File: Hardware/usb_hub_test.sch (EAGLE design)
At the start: 99 parts, among them CN1 54819-0519, CN2 TSW-120-08-L-S-RA, CN4 1-1734530-1, IC1 FT230XQ, IC2 TUSB2046BIRHBT, IC3 MAX3375, IC4 PIC24FJ128GA202-I/MM, IC5 FT230XQ, IC7 MAX3375

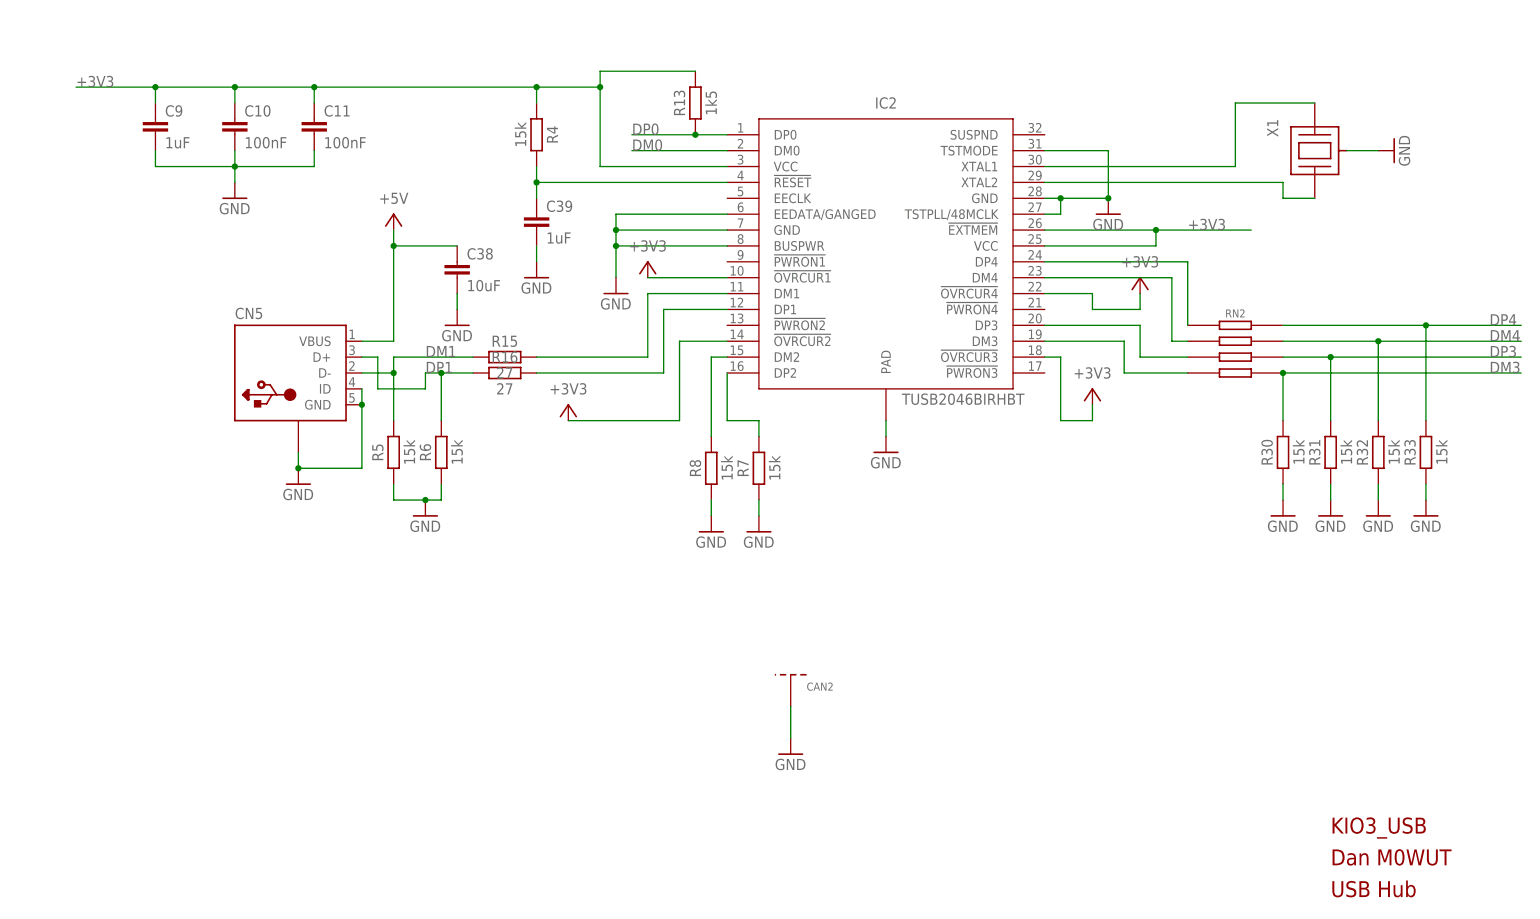
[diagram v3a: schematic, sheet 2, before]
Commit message: Implementing Board changes from v1
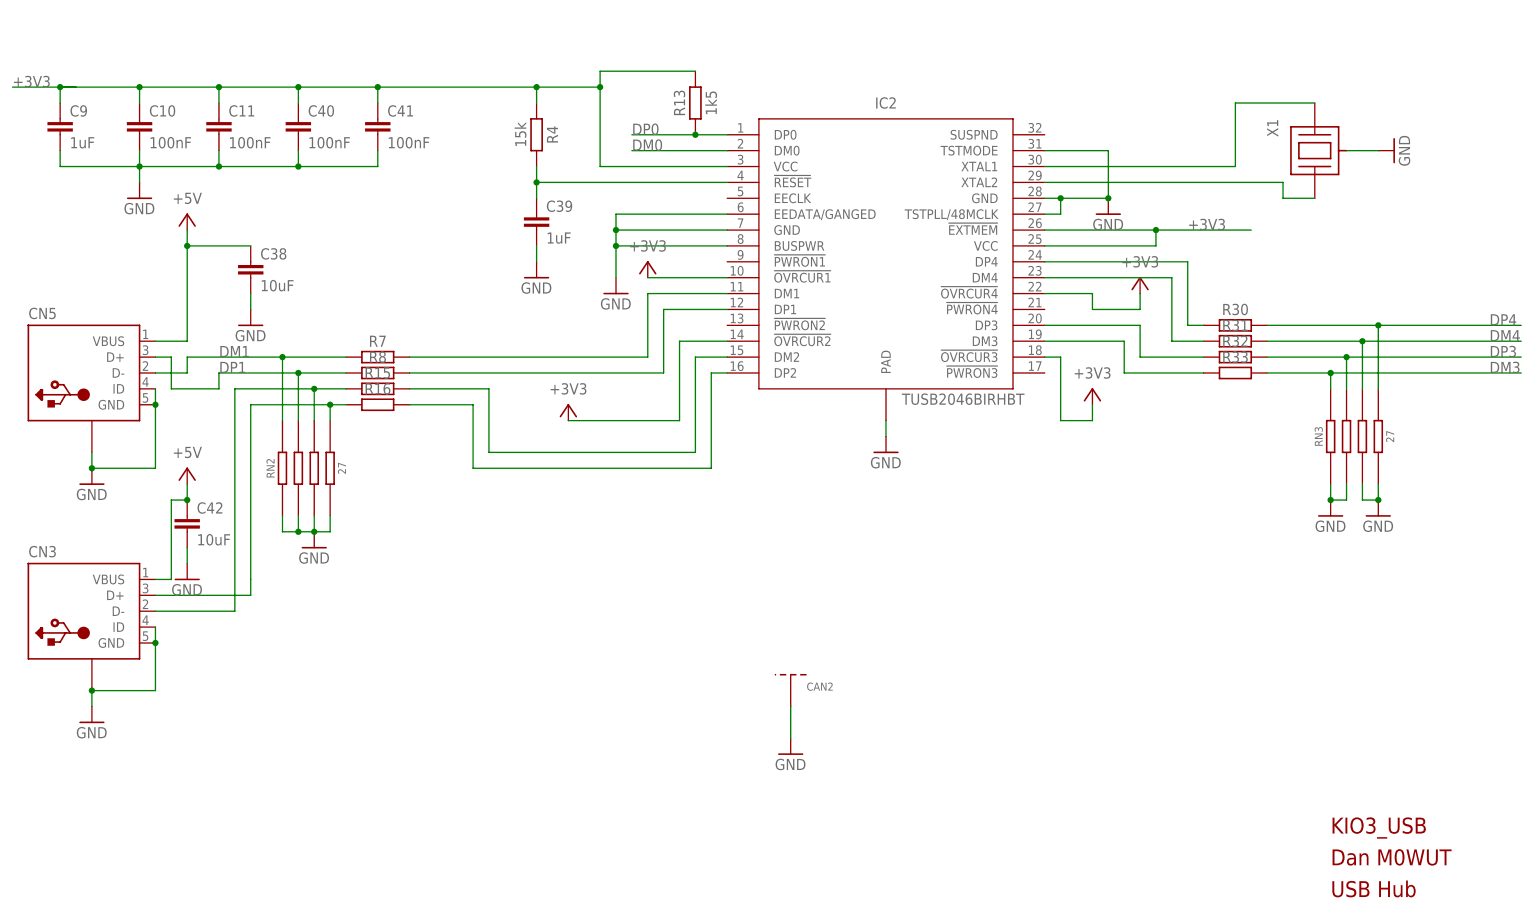
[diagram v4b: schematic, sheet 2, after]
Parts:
- removed C1, C35, C37: 100nF, rcl:C-EUC0402
- removed C27, C28, C33, C34: 1nF, rcl:C-EUC0402
- removed D2, D3: BZT52C4V7-7-F, adafruit:DIODESOD-123
- removed IC3, IC7: MAX3375, m0wut:IC_MAX3375
- removed L2, L3, L5, L6: 100uH, m0wut:INDUCTOR
- removed R12, R3: 220, rcl:R-EU_R0402
- removed R5, R6: 15k, rcl:R-EU_R0402
- added C40, C41: 100nF, rcl:C-EUC0402
- added C42: 10uF, rcl:C-EUC0805
- added CN3: (no value), m0wut:USBOTG_VERTICAL
- added Q1, Q2: (no value), adafruit:MOSFET-NREFLOW
- added RN3: 27, m0wut:R_BOURNS_CAY16-J4
- added RN4: (no value), m0wut:R_BOURNS_CAY16-J4
- R15, R16: value 27 -> (none)
- R30, R31, R32, R33, R7, R8: value 15k -> (none)
- RN2: value (none) -> 27
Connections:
- removed net N$188: IC3.OH, L2.1
- removed net N$189: D2.C, IC3.IH, R12.1
- removed net N$4: D3.C, IC7.IH, R3.1
- removed net N$5: IC7.OH, L5.1
- removed net N$6: L3.1, R12.2
- removed net N$7: L6.1, R3.2
- removed net P3_RXD: C27.1, L5.2, U$1.1
- removed net P3_TXD: C28.1, L6.2, U$1.3
- new net N$18: CN3.D-, R15.1, RN2.3A
- new net N$19: CN3.D+, R16.1, RN2.4A
- net +3V3: now also C40.1, C41.1, RN4.2A; no longer C1.1, C35.1, IC3.EN, IC3.VL, IC7.EN, IC7.VL
- net +5V: now also C42.1, CN3.VBUS, RN4.3A; no longer C37.1, IC3.VH, IC7.VH
- net 232_RXD: now also Q2.G, RN4.1; no longer C33.1, L2.2
- net 232_TXD: now also Q1.D, RN4.3; no longer C34.1, L3.2
- net DM1: now also R7.1, RN2.1A; no longer R15.1, R5.2
- net DM3: now also R33.2, RN3.1A; no longer R30.2, RN2.4A
- net DM4: now also R31.2, RN3.3A; no longer R32.2, RN2.2A
- net DP1: now also R8.1, RN2.2A; no longer R16.1, R6.2
- net DP3: now also R32.2, RN3.2A; no longer R31.2, RN2.3A
- net DP4: now also R30.2, RN3.4A; no longer R33.2, RN2.1A
- net GND: now also C40.2, C41.2, C42.2, CN3.GND, CN3.ID, CN3.SHIELD, Q1.S, Q2.S, RN2.1, RN2.2, RN2.3, RN2.4, RN3.1, RN3.2, RN3.3, RN3.4, RN4.1A, RN4.4; no longer C1.2, C27.2, C28.2, C33.2, C34.2, C35.2, C37.2, D2.A, D3.A, IC3.GND, IC7.GND, R30.1, R31.1, R32.1, R33.1, R5.1, R6.1, R7.1, R8.1
- net N$1: now also R31.1; no longer RN2.2
- net N$11: now also R15.2; no longer R8.2
- net N$12: now also R7.2; no longer R15.2
- net N$13: now also R8.2; no longer R16.2
- net N$14: now also R16.2; no longer R7.2
- net N$16: now also R32.1; no longer RN2.3
- net N$17: now also R33.1; no longer RN2.4
- net N$3: now also R30.1; no longer RN2.1
- net UART_FROM_K3: now also Q2.D, RN4.2; no longer IC3.OL
- net UART_FROM_P3: no longer IC7.OL
- net UART_TO_K3: now also Q1.G, RN4.4A; no longer IC3.IL
- net UART_TO_P3: no longer IC7.IL
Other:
- note removed: "Inverted UART (Compliant with RS232)"
- moved on the sheet: C10, C11, C38, C9, CN5, R15, R16, R30, R31, R32, R33, R7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

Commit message: v2 pcb ordered
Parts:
- removed CAN2: CAN_MASTECH, m0wut:CAN_MASTECH
- added C1, C35, C37: 100nF, rcl:C-EUC0402
- added C27, C28, C33, C43, C44: 1nF, rcl:C-EUC0402
- added C34: 10uF, rcl:C-EUC0805
- added IC3: IC_MAX3313, m0wut:IC_MAX3313
- added L2, L3, L5, L6: (no value), m0wut:INDUCTOR
- added R3: 0R, rcl:R-EU_R0402
- C42: value 10uF -> 100nF; device rcl:C-EUC0805 -> rcl:C-EUC0402
- CN3: value (none) -> 48204-0001; device m0wut:USBOTG_VERTICAL -> m0wut:USB_4WAY""
- CN5: device m0wut:USBOTG_VERTICAL -> m0wut:USBWURTH
- L1: value 100uH -> (none)
- RN4: value (none) -> 10k
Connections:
- removed net N$18: CN3.D-, R15.1, RN2.3A
- removed net N$19: CN3.D+, R16.1, RN2.4A
- new net 232_FROM_P3: C44.1, L5.2, U$1.3
- new net 232_TO_P3: C43.1, L1.2, U$1.1
- new net AGND: C12.2, C13.2, C14.2, C15.2, C16.2, C17.2, C18.2, C19.2, C20.2, C21.2, C22.2, C23.2, C24.2, C27.2, C28.2, C33.2, C43.2, C44.2, CN4.TAB, U$1.TAB
- new net ASDF: L3.1, Q1.D, RN4.3
- new net DM2: CN5.D-, R15.1, RN2.3A
- new net DP2: CN5.D+, R16.1, RN2.4A
- new net N$15: C37.1, IC3.V-
- new net N$4: C42.1, IC3.VCC, L6.2
- new net N$6: C35.1, IC3.C1-
- new net N$7: C35.2, IC3.C1+
- new net SADF: L2.1, Q2.G, RN4.2
- new net WTRE: IC3.TOUT, L1.1
- new net Y5W4: IC3.RIN, L5.1
- net +3V3: now also C1.1, RN4.1A; no longer RN4.2A
- net +5V: now also C34.1, L6.1; no longer C42.1
- net 232_RXD: now also C28.1, L2.2; no longer Q2.G, RN4.1
- net 232_TXD: now also C27.1, L3.2; no longer Q1.D, RN4.3
- net ACC_COMMON: now also C33.1, R3.2; no longer L1.2
- net DM1: now also CN3.D-; no longer CN5.D-
- net DP1: now also CN3.D+; no longer CN5.D+
- net GND: now also C1.2, C34.2, C37.2, IC3.GND, R3.1, RN4.2A, RN4.4A; no longer C12.2, C13.2, C14.2, C15.2, C16.2, C17.2, C18.2, C19.2, C20.2, C21.2, C22.2, C23.2, C24.2, CAN2.P$1, CN3.ID, CN4.TAB, L1.1, RN4.1A, RN4.4, U$1.TAB
- net UART_FROM_K3: now also RN4.1; no longer RN4.2
- net UART_FROM_P3: now also IC3.ROUT
- net UART_TO_K3: now also RN4.4; no longer RN4.4A
- net UART_TO_P3: now also IC3.TIN
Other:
- note added: "Audio Codec"
- note removed: "Pickit 3"
